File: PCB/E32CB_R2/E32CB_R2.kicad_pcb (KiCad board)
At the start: 2 copper layers, 111.3 x 90.9 mm, 89 parts, among them J1 GPIO_HEADER, J10 S, J11 Q4, J12 S, J13 Q3, J14 S, J15 Q8, J16 S, J17 Q7, J18 S, J19 Q6, J2 Power, J20 S, J21 Q5, J22 S, J3 USB_B, J4 USB +5V, J5 NEXTION, J6 I2C, J7 Q1, J8 S, J9 Q2, Q1 S8050, Q10 IRLR2905, Q2 S8050, Q3 IRLR2905, Q4 IRLR2905, Q5 IRLR2905, Q6 IRLR2905, Q7 IRLR2905, Q8 IRLR2905, Q9 IRLR2905, U1 ESP32-WROOM-32, X1 12MHz

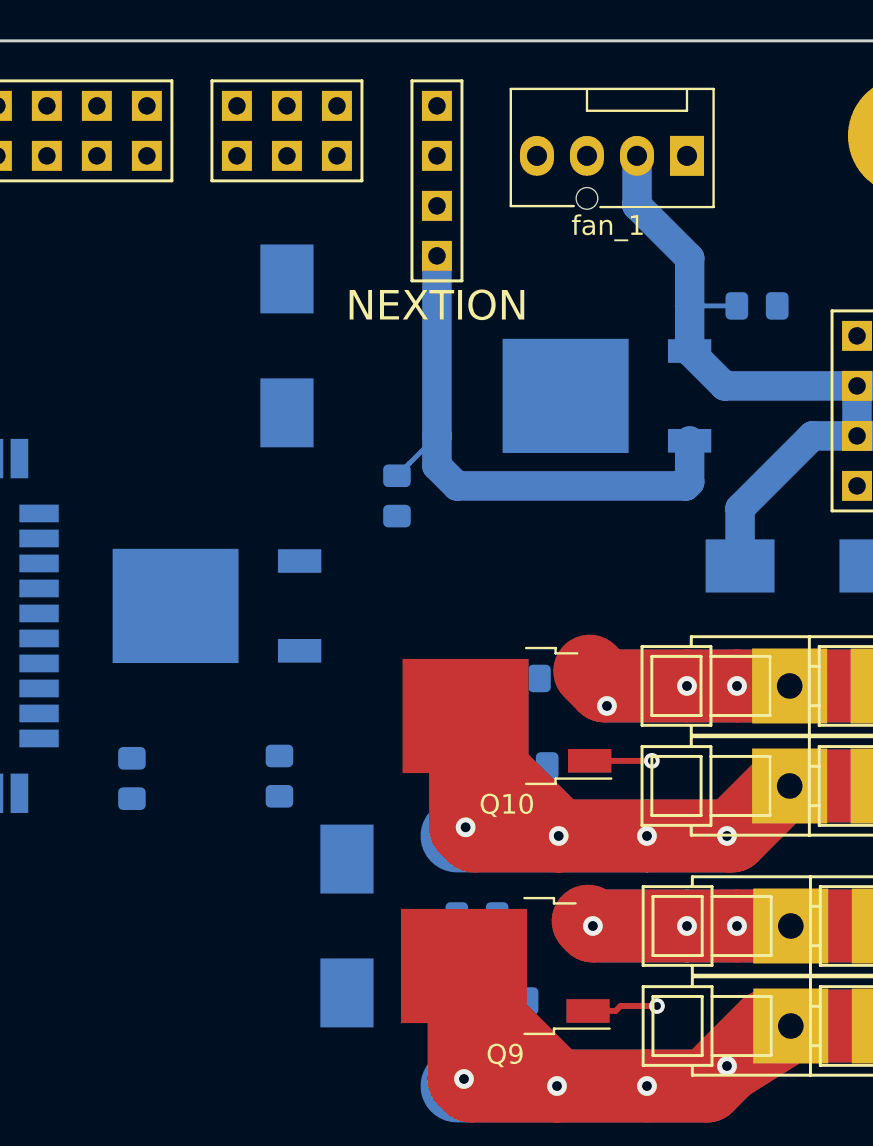
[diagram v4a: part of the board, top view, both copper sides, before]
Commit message: diodes connection
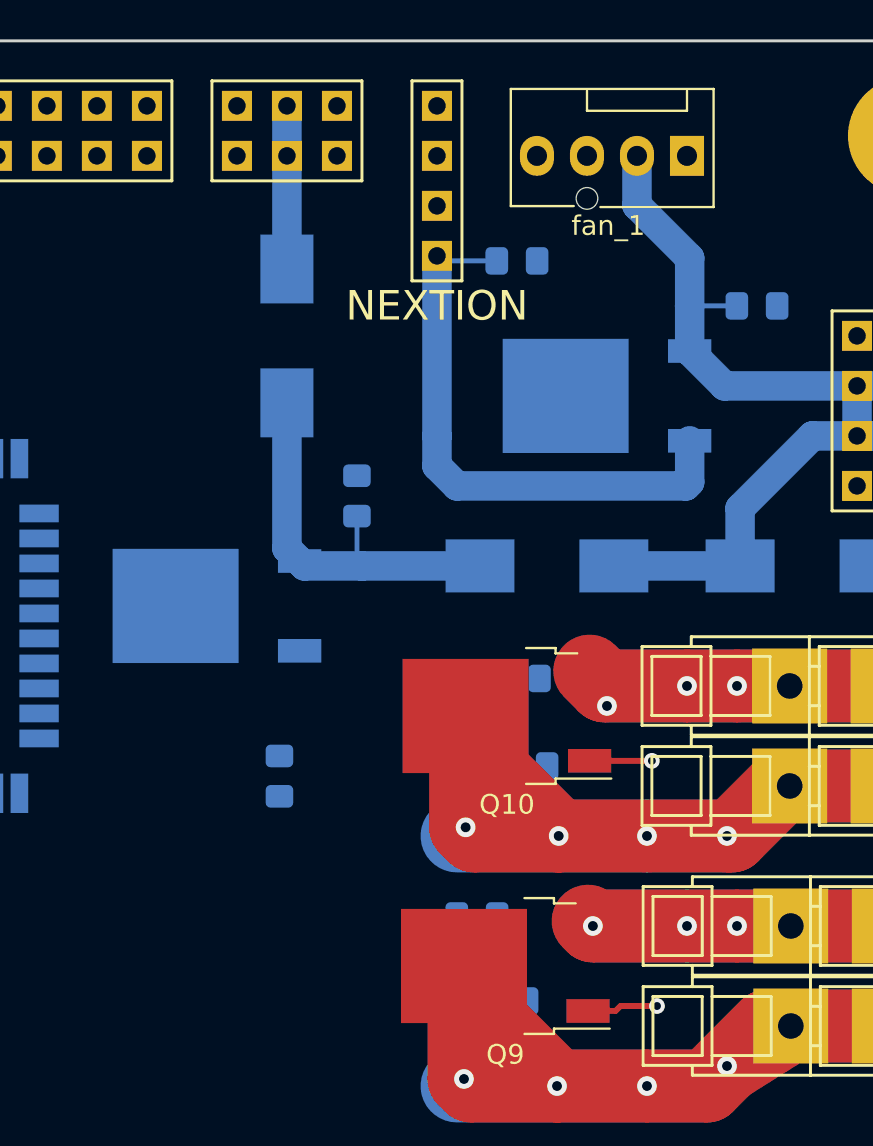
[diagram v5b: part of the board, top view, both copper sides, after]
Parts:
- moved D3 20.9 mm to (184.9, 72.6), turned to 0 degrees
- moved C8 18.3 mm to (175.3, 69.1)
- moved C7 13.4 mm to (183.4, 57.1), turned to 0 degrees
- moved D2 0.51 mm to (171.7, 61.0)
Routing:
- net Net-(3V3stabilizer1-Pad1): track 0.00 -> 20.2 mm
- net +5V: track 0.00 -> 8.28 mm
- net +12V: track 45.7 -> 52.1 mm
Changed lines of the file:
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@@
     (thickness 1.6)
     (drawings 8)
-    (tracks 431)
+    (tracks 439)
     (zones 0)
     (modules 89)
@@
   )
   (setup
-    (last_trace_width 1.5)
+    (last_trace_width 0.25)
     (user_trace_width 0.3)
     (user_trace_width 0.5)
@@
     (solder_mask_min_width 0.25)
     (aux_axis_origin 0 0)
-    (visible_elements FFFFFF7F)
+    (visible_elements FFFFF77F)
     (pcbplotparams
       (layerselection 0x010fc_ffffffff)
@@
   )
   (module Capacitor_SMD:C_0805_2012Metric_Pad1.15x1.40mm_HandSolder (layer B.Cu)
-    (at 177.292 69.088 270)
+    (at 183.388 57.15)
     (descr "Capacitor SMD 0805 (2012 Metric), square (rectangular) end terminal, IPC_7351 nominal with elongated pad for handsoldering. (Body size source: https://docs.google.com/spreadsheets/d/1BsfQQcO9C6DZCsRaXUlFlo91Tg2WpOkGARC1WS5S8t0/edit?usp=sharing), generated with kicad-footprint-generator")
     (tags "capacitor handsolder")
     (attr smd)
-    (fp_text reference C7 (at 0 1.65 270) (layer B.SilkS)
+    (fp_text reference C7 (at 0 -1.778) (layer B.SilkS)
       (effects (font (size 1 1) (thickness 0.15)) (justify mirror))
     )
-    (fp_text value 100nF (at 0 -1.65 270) (layer B.Fab)
+    (fp_text value 100nF (at 0 -1.65) (layer B.Fab)
       (effects (font (size 1 1) (thickness 0.15)) (justify mirror))
     )
@@
     (fp_line (start 1.85 0.95) (end 1.85 -0.95) (layer B.CrtYd) (width 0.05))
     (fp_line (start 1.85 -0.95) (end -1.85 -0.95) (layer B.CrtYd) (width 0.05))
-    (fp_text user %R (at 0 0 270) (layer B.Fab)
+    (fp_text user %R (at 0 0) (layer B.Fab)
       (effects (font (size 0.5 0.5) (thickness 0.08)) (justify mirror))
     )
-    (pad 1 smd roundrect (at -1.025 0 270) (size 1.15 1.4) (layers B.Cu B.Paste B.Mask) (roundrect_rratio 0.217391)
+    (pad 1 smd roundrect (at -1.025 0) (size 1.15 1.4) (layers B.Cu B.Paste B.Mask) (roundrect_rratio 0.217391)
       (net 68 /display_Vin))
-    (pad 2 smd roundrect (at 1.025 0 270) (size 1.15 1.4) (layers B.Cu B.Paste B.Mask) (roundrect_rratio 0.217391)
+    (pad 2 smd roundrect (at 1.025 0) (size 1.15 1.4) (layers B.Cu B.Paste B.Mask) (roundrect_rratio 0.217391)
       (net 8 GND))
     (model ${KISYS3DMOD}/Capacitor_SMD.3dshapes/C_0805_2012Metric.wrl
@@
   )
   (module Capacitor_SMD:C_0805_2012Metric_Pad1.15x1.40mm_HandSolder (layer B.Cu)
-    (at 163.83 83.439 90)
+    (at 175.26 69.088 90)
     (descr "Capacitor SMD 0805 (2012 Metric), square (rectangular) end terminal, IPC_7351 nominal with elongated pad for handsoldering. (Body size source: https://docs.google.com/spreadsheets/d/1BsfQQcO9C6DZCsRaXUlFlo91Tg2WpOkGARC1WS5S8t0/edit?usp=sharing), generated with kicad-footprint-generator")
     (tags "capacitor handsolder")
@@
   )
   (module Diode_SMD:D_MELF_Handsoldering (layer B.Cu)
-    (at 174.752 90.932 90)
+    (at 184.912 72.644)
     (descr "Diode MELF Handsoldering")
     (tags "Diode MELF Handsoldering")
     (attr smd)
-    (fp_text reference D3 (at 0 2.25 90) (layer B.SilkS)
+    (fp_text reference D3 (at 0 2.25) (layer B.SilkS)
       (effects (font (size 1 1) (thickness 0.15)) (justify mirror))
     )
-    (fp_text value 1N4007 (at 0 -2.25 90) (layer B.Fab)
+    (fp_text value 1N4007 (at 0 -2.25) (layer B.Fab)
       (effects (font (size 1 1) (thickness 0.15)) (justify mirror))
     )
-    (fp_text user %R (at 0 2.25 90) (layer B.Fab)
+    (fp_text user %R (at 0 2.25) (layer B.Fab)
       (effects (font (size 1 1) (thickness 0.15)) (justify mirror))
     )
@@
     (fp_line (start 5.4 -1.6) (end -5.4 -1.6) (layer B.CrtYd) (width 0.05))
     (fp_line (start -5.4 -1.6) (end -5.4 1.6) (layer B.CrtYd) (width 0.05))
-    (pad 1 smd rect (at -3.4 0 90) (size 3.5 2.7) (layers B.Cu B.Paste B.Mask)
+    (pad 1 smd rect (at -3.4 0) (size 3.5 2.7) (layers B.Cu B.Paste B.Mask)
       (net 63 "Net-(3V3stabilizer1-Pad1)"))
-    (pad 2 smd rect (at 3.4 0 90) (size 3.5 2.7) (layers B.Cu B.Paste B.Mask)
+    (pad 2 smd rect (at 3.4 0) (size 3.5 2.7) (layers B.Cu B.Paste B.Mask)
       (net 69 +12V))
     (model ${KISYS3DMOD}/Diode_SMD.3dshapes/D_MELF.wrl
@@
   )
   (module Diode_SMD:D_MELF_Handsoldering (layer B.Cu)
-    (at 171.704 61.468 90)
+    (at 171.704 60.96 90)
     (descr "Diode MELF Handsoldering")
     (tags "Diode MELF Handsoldering")
@@
   (segment (start 119.126 115.872) (end 119.629 115.369) (width 3.7) (layer F.Cu) (net 43))
   (via (at 119.126 115.872) (size 1) (drill 0.5) (layers F.Cu B.Cu) (net 43))
+  (segment (start 171.704 71.752) (end 172.348 72.396) (width 1.5) (layer B.Cu) (net 63))
+  (segment (start 171.704 64.36) (end 171.704 71.752) (width 1.5) (layer B.Cu) (net 63))
+  (segment (start 172.596 72.644) (end 172.348 72.396) (width 1.5) (layer B.Cu) (net 63))
+  (segment (start 175.26 72.39) (end 175.514 72.644) (width 0.25) (layer B.Cu) (net 63))
+  (segment (start 181.512 72.644) (end 175.514 72.644) (width 1.5) (layer B.Cu) (net 63))
+  (segment (start 175.26 70.113) (end 175.26 72.39) (width 0.25) (layer B.Cu) (net 63))
+  (segment (start 175.514 72.644) (end 172.596 72.644) (width 1.5) (layer B.Cu) (net 63))
   (segment (start 145.288 131.007) (end 145.288 126.007) (width 3.7) (layer F.Cu) (net 64))
   (segment (start 145.288 126.007) (end 143.51 123.317) (width 3.7) (layer F.Cu) (net 64))
@@
   (segment (start 191.968 68.58) (end 180.34 68.58) (width 1.5) (layer B.Cu) (net 68))
   (segment (start 180.34 68.58) (end 179.324 67.564) (width 1.5) (layer B.Cu) (net 68))
-  (segment (start 177.924372 67.439628) (end 179.324 66.04) (width 0.25) (layer B.Cu) (net 68))
   (segment (start 179.324 67.564) (end 179.324 66.04) (width 1.5) (layer B.Cu) (net 68))
-  (segment (start 177.915372 67.439628) (end 177.924372 67.439628) (width 0.25) (layer B.Cu) (net 68))
-  (segment (start 177.292 68.063) (end 177.915372 67.439628) (width 0.25) (layer B.Cu) (net 68))
   (segment (start 179.324 66.04) (end 179.324 56.896) (width 1.5) (layer B.Cu) (net 68))
+  (segment (start 179.578 57.15) (end 179.324 56.896) (width 0.25) (layer B.Cu) (net 68))
+  (segment (start 182.363 57.15) (end 179.578 57.15) (width 0.25) (layer B.Cu) (net 68))
   (segment (start 203.2 63.5) (end 200.66 63.5) (width 1.5) (layer B.Cu) (net 69))
   (segment (start 200.66 63.5) (end 200.66 66.04) (width 1.5) (layer B.Cu) (net 69))
@@
   (segment (start 198.398 66.04) (end 200.938 66.04) (width 1.5) (layer B.Cu) (net 69))
   (segment (start 194.72 69.718) (end 198.398 66.04) (width 1.5) (layer B.Cu) (net 69))
+  (segment (start 194.72 72.644) (end 188.312 72.644) (width 1.5) (layer B.Cu) (net 69))
   (segment (start 188.468 131.04) (end 188.468 126.04) (width 3.7) (layer F.Cu) (net 70))
   (segment (start 188.468 126.04) (end 186.69 123.19) (width 3.7) (layer F.Cu) (net 70))
@@
   (segment (start 119.2845 93.472) (end 119.2845 92.222) (width 0.25) (layer B.Cu) (net 77))
   (segment (start 119.2845 92.222) (end 121.093 90.4135) (width 0.25) (layer B.Cu) (net 77))
+  (segment (start 171.704 49.276) (end 171.704 57.56) (width 1.5) (layer B.Cu) (net 83))
   (segment (start 112.268 99.051) (end 112.259 99.06) (width 1.5) (layer B.Cu) (net 84))
   (segment (start 112.268 92.456) (end 112.268 99.051) (width 1.5) (layer B.Cu) (net 84))

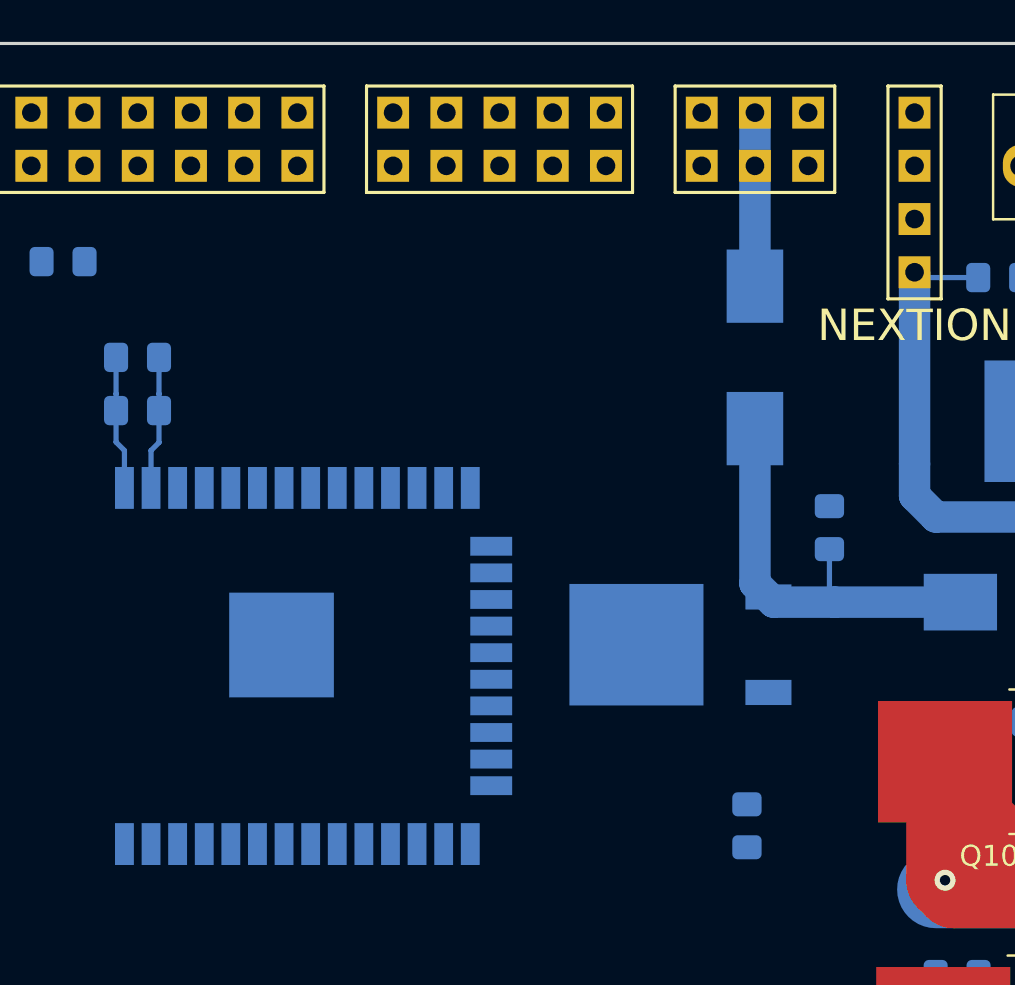
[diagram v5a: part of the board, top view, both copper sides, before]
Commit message: 3v3 update
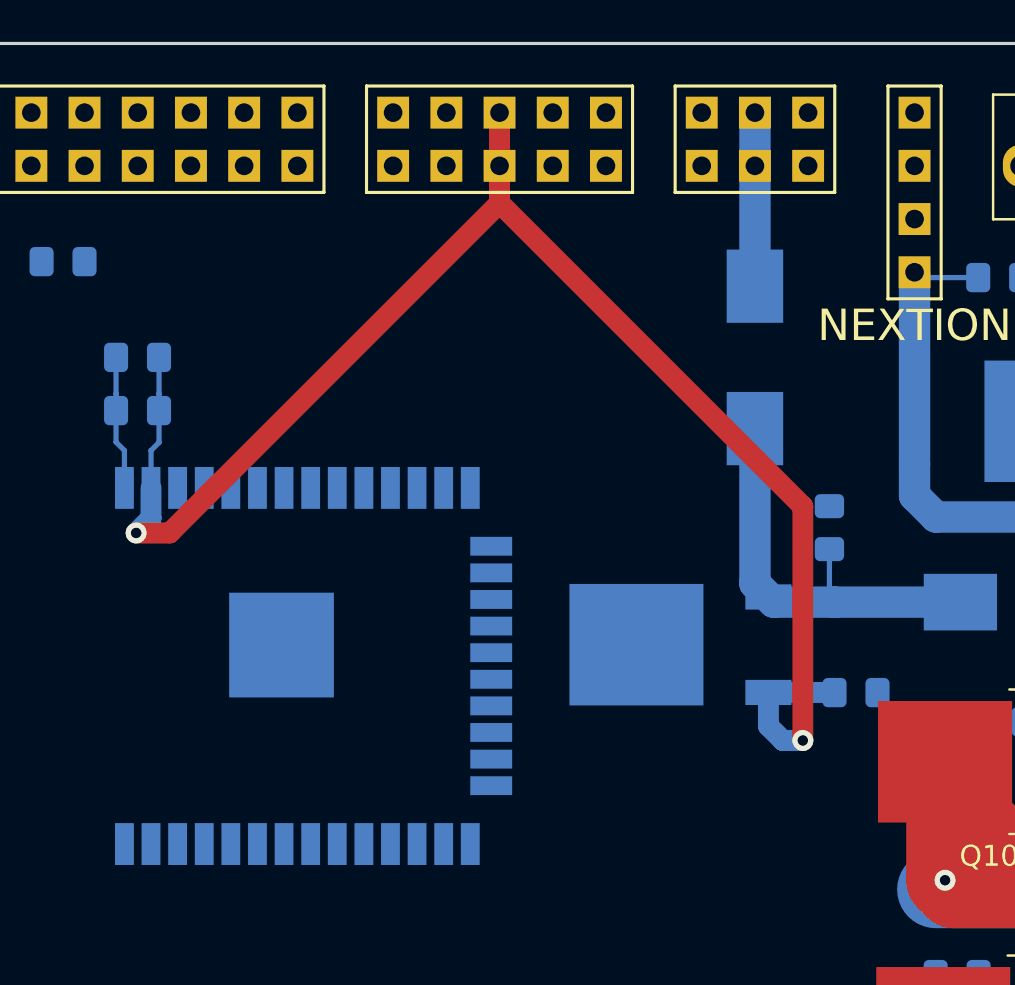
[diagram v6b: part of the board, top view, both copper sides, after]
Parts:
- moved C9 8.22 mm to (176.5, 77.0), turned to 0 degrees
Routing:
- net +3V3: track 6.39 -> 76.3 mm, vias 0 -> 2
